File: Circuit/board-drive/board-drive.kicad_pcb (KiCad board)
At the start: 2 copper layers, 164.3 x 98.3 mm, 33 parts, among them M3 MountingHole_3.2mm_M3, P1 XT30, P10 XT60, P2 XT30, P3 XT30, P4 XT30, P5 XT30, P6 XT30, P7 XT30, P8 XT30, P9 XT60, U1 Pololu_Maestro12, U10 PowerDist_WiretoBoard, U11 PowerDist_WiretoBoard, U16 PowerDist_WiretoBoard, U17 PowerDist_WiretoBoard, U18 PowerDist_WiretoBoard, U19 PowerDist_WiretoBoard, U2 Si8660BA-B-IS1, U3 Si8660BA-B-IS1, U8 PowerDist_WiretoBoard, U9 PowerDist_WiretoBoard

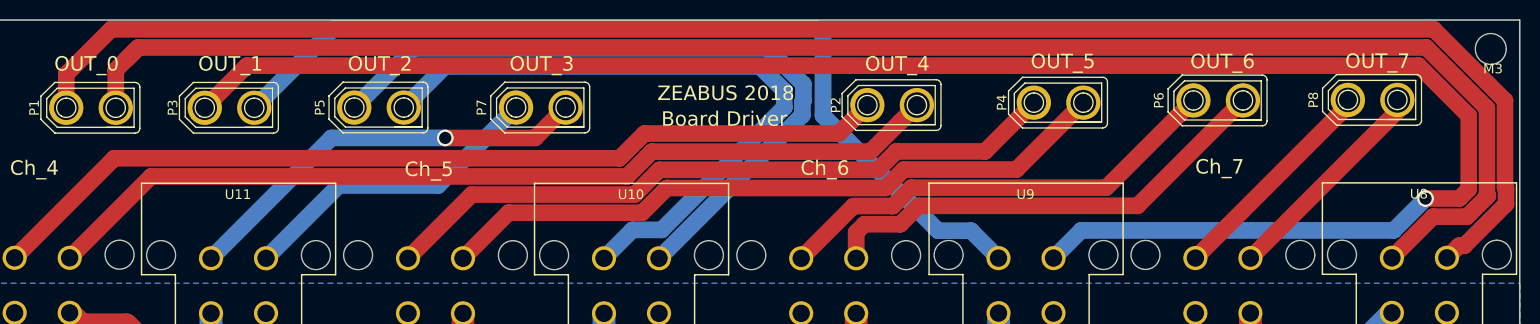
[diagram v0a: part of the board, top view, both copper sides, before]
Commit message: fix wire near to the edge cut and generate new gerberfile
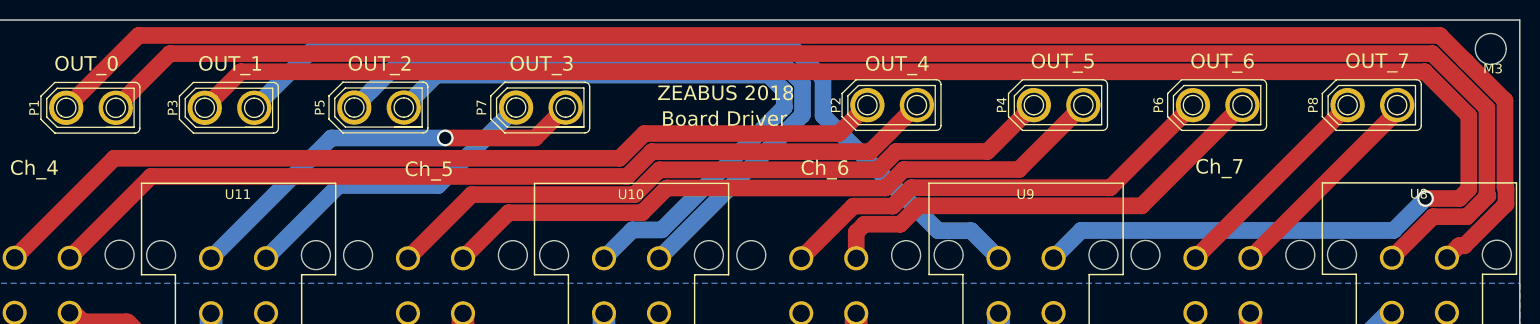
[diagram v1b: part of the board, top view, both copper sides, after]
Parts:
- moved P8 0.53 mm to (199.3, 60.7)
- moved P6 0.49 mm to (183.3, 60.7)
- moved P4 0.25 mm to (166.8, 60.7)
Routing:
- net /OUTA_0: track 174.0 -> 168.5 mm
- net /OUTA_1: track 95.3 -> 91.7 mm
- net /OUTB_0: track 176.7 -> 174.2 mm
- net /OUTB_2: track 74.9 -> 74.0 mm
- net /OUTA_2: track 69.4 -> 68.6 mm
- net /OUTA_7: track 22.7 -> 23.3 mm
- net /OUTB_1: track 188.5 -> 188.0 mm
